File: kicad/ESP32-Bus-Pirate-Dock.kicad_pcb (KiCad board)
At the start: 4 copper layers, 80 x 73.8 mm, 39 parts, among them CN1 HX25418-10WA, J1 Conn_01x22, J2 Conn_01x22, J3 Conn_01x10V, J4 Conn_01x22, J5 Conn_01x22, J6 Conn_01x22, J7 Conn_02x03, Q1 2N7002, SW1 TA-3532S-A2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

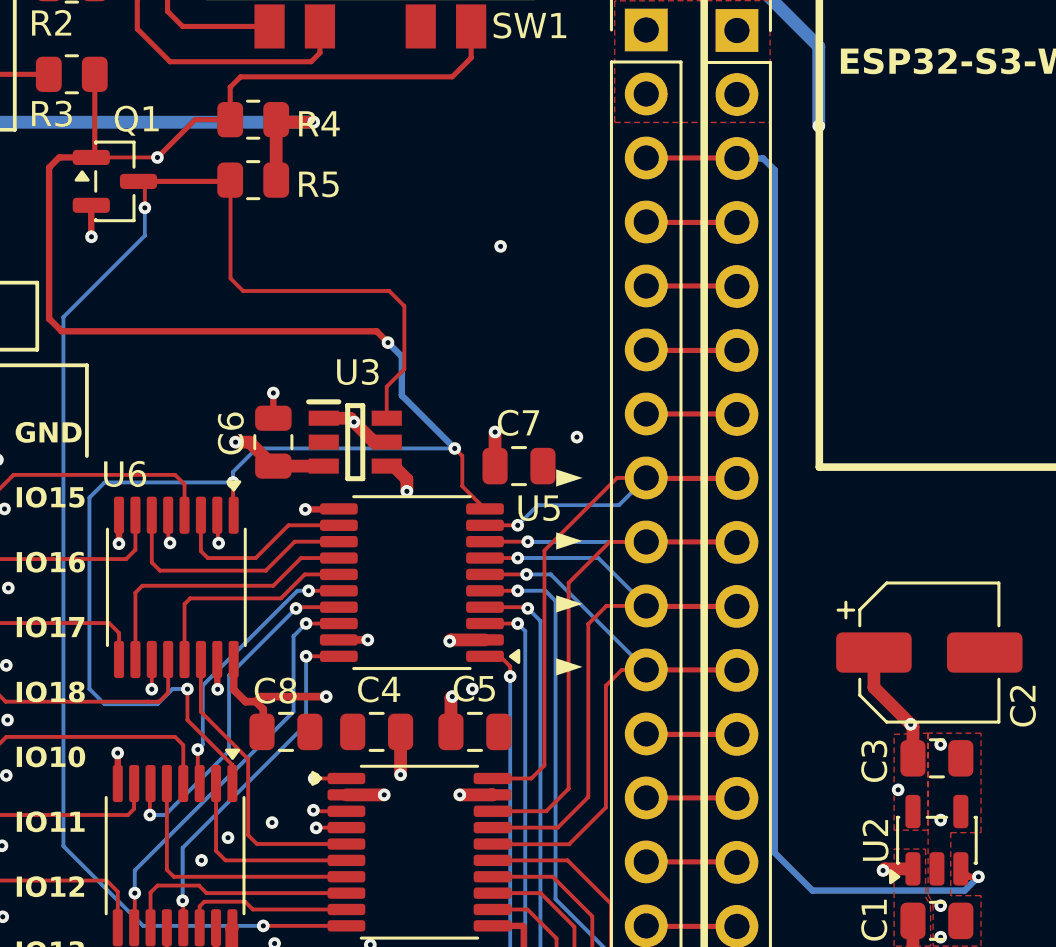
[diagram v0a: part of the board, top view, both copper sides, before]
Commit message: Deleted vias & added thermal relief spoke
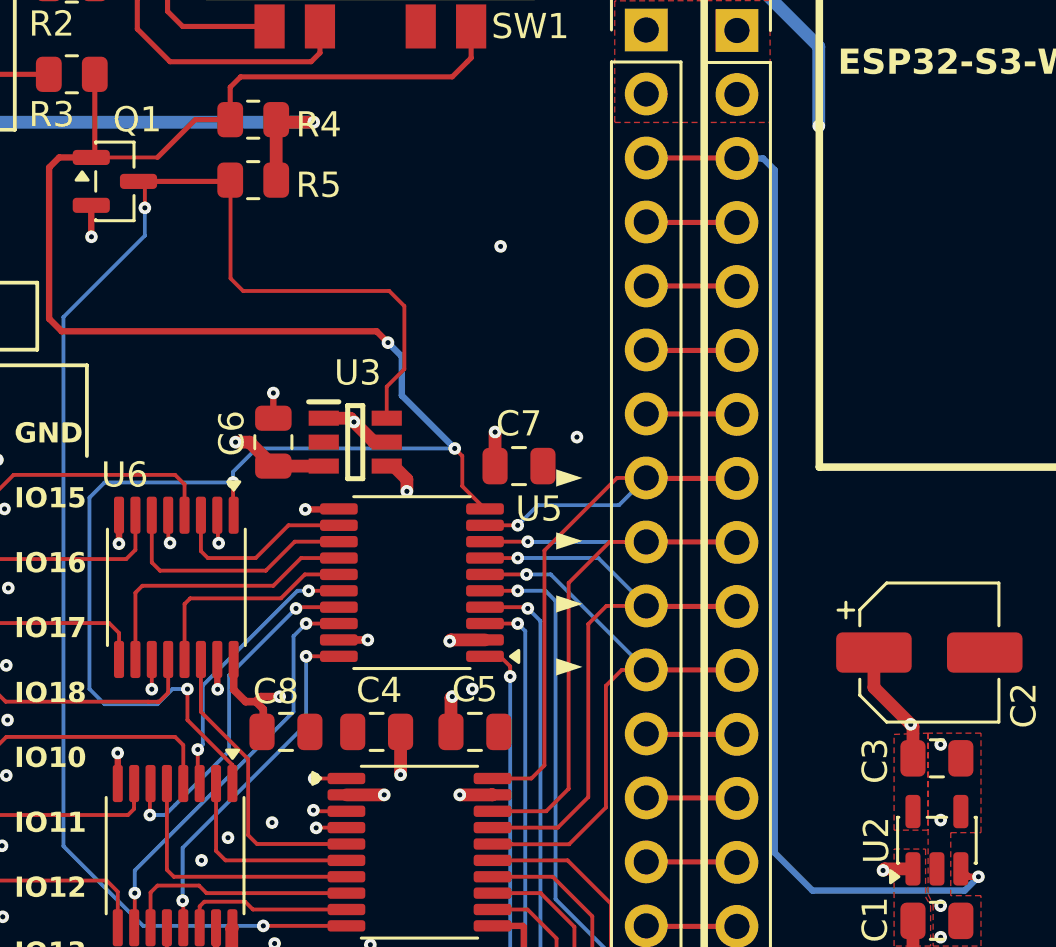
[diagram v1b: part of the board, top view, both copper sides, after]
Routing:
- net /Voltage Level Translator/SEL: vias 5 -> 4
- net +1V8: vias 7 -> 6
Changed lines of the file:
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@@
+	)
+	(segment
+		(start 152.45 96.9)
+		(end 151.7 96.9)
+		(width 0.3048)
+		(layer "F.Cu")
+		(net 11)
 	)
 	(segment
@@
 		(end 155.25 85.85)
 		(width 0.508)
-		(layer "F.Cu")
-		(net 11)
-	)
-	(segment
-		(start 151.7 96.9)
-		(end 154.3 96.9)
-		(width 0.3048)
 		(layer "F.Cu")
 		(net 11)
@@
 	)
 	(segment
+		(start 151.7 96.9)
+		(end 151.5 97.1)
+		(width 0.3048)
+		(layer "F.Cu")
+		(net 11)
+	)
+	(segment
 		(start 159.25 94.65)
 		(end 159.2 94.7)
@@
 		(net 11)
 	)
-	(segment
-		(start 151.5 97.1)
-		(end 151.7 96.9)
-		(width 0.3048)
-		(layer "F.Cu")
-		(net 11)
-	)
 	(via
 		(at 155.4 86)
@@
 	)
 	(via
-		(at 154.3 96.9)
+		(at 152.45 96.9)
 		(size 0.5)
 		(drill 0.2)
@@
 	)
 	(segment
+		(start 158.3 96.9)
+		(end 158.3 94.2)
+		(width 0.508)
+		(layer "In2.Cu")
+		(net 11)
+	)
+	(segment
+		(start 158.3 100)
+		(end 158.3 99.5)
+		(width 0.508)
+		(layer "In2.Cu")
+		(net 11)
+	)
+	(segment
+		(start 156.2 86.8)
+		(end 155.4 86)
+		(width 0.508)
+		(layer "In2.Cu")
+		(net 11)
+	)
+	(segment
+		(start 159.1 100.8)
+		(end 158.3 100)
+		(width 0.508)
+		(layer "In2.Cu")
+		(net 11)
+	)
+	(segment
+		(start 166.2 63)
+		(end 167 63.8)
+		(width 0.508)
+		(layer "In2.Cu")
+		(net 11)
+	)
+	(segment
+		(start 161 86.4)
+		(end 159.1 88.3)
+		(width 0.508)
+		(layer "In2.Cu")
+		(net 11)
+	)
+	(segment
+		(start 158 74.1)
+		(end 159.12 72.98)
+		(width 0.508)
+		(layer "In2.Cu")
+		(net 11)
+	)
+	(segment
+		(start 167 63.8)
+		(end 167 70.44)
+		(width 0.508)
+		(layer "In2.Cu")
+		(net 11)
+	)
+	(segment
+		(start 158.8 94.7)
+		(end 158.3 94.2)
+		(width 0.508)
+		(layer "In2.Cu")
+		(net 11)
+	)
+	(segment
+		(start 159.6 100.8)
+		(end 159.1 100.8)
+		(width 0.508)
+		(layer "In2.Cu")
+		(net 11)
+	)
+	(segment
+		(start 158.3 122.43)
+		(end 158.3 107.5)
+		(width 0.508)
+		(layer "In2.Cu")
+		(net 11)
+	)
+	(segment
+		(start 158.3 99.5)
+		(end 158.3 107.5)
+		(width 0.508)
+		(layer "In2.Cu")
+		(net 11)
+	)
+	(segment
+		(start 158.7 96.9)
+		(end 159.3 96.9)
+		(width 0.508)
+		(layer "In2.Cu")
+		(net 11)
+	)
+	(segment
+		(start 158.2 74.1)
+		(end 158 74.1)
+		(width 0.508)
+		(layer "In2.Cu")
+		(net 11)
+	)
+	(segment
+		(start 158.3 94.2)
+		(end 158.3 88.3)
+		(width 0.508)
+		(layer "In2.Cu")
+		(net 11)
+	)
+	(segment
+		(start 158.2 87.4)
+		(end 158.2 74.1)
+		(width 0.508)
+		(layer "In2.Cu")
+		(net 11)
+	)
+	(segment
+		(start 158.3 107.5)
+		(end 157.6 108.2)
+		(width 0.508)
+		(layer "In2.Cu")
+		(net 11)
+	)
+	(segment
+		(start 154.1 63)
+		(end 166.2 63)
+		(width 0.508)
+		(layer "In2.Cu")
+		(net 11)
+	)
+	(segment
 		(start 158.3 96.5)
 		(end 158.7 96.9)
@@
 	)
 	(segment
-		(start 158.3 96.9)
-		(end 158.3 94.2)
-		(width 0.508)
-		(layer "In2.Cu")
-		(net 11)
-	)
-	(segment
-		(start 158.3 100)
-		(end 158.3 99.5)
-		(width 0.508)
-		(layer "In2.Cu")
-		(net 11)
-	)
-	(segment
-		(start 156.2 86.8)
-		(end 155.4 86)
-		(width 0.508)
-		(layer "In2.Cu")
-		(net 11)
-	)
-	(segment
-		(start 159.1 100.8)
-		(end 158.3 100)
-		(width 0.508)
-		(layer "In2.Cu")
-		(net 11)
-	)
-	(segment
-		(start 166.2 63)
-		(end 167 63.8)
-		(width 0.508)
-		(layer "In2.Cu")
-		(net 11)
-	)
-	(segment
-		(start 161 86.4)
-		(end 159.1 88.3)
-		(width 0.508)
-		(layer "In2.Cu")
-		(net 11)
-	)
-	(segment
-		(start 154.3 96.9)
-		(end 157.9 96.9)
-		(width 0.508)
-		(layer "In2.Cu")
-		(net 11)
-	)
-	(segment
-		(start 158 74.1)
-		(end 159.12 72.98)
-		(width 0.508)
-		(layer "In2.Cu")
-		(net 11)
-	)
-	(segment
-		(start 167 63.8)
-		(end 167 70.44)
-		(width 0.508)
-		(layer "In2.Cu")
-		(net 11)
-	)
-	(segment
-		(start 158.8 94.7)
-		(end 158.3 94.2)
-		(width 0.508)
-		(layer "In2.Cu")
-		(net 11)
-	)
-	(segment
-		(start 159.6 100.8)
-		(end 159.1 100.8)
-		(width 0.508)
-		(layer "In2.Cu")
-		(net 11)
-	)
-	(segment
-		(start 158.3 122.43)
-		(end 158.3 107.5)
-		(width 0.508)
-		(layer "In2.Cu")
-		(net 11)
-	)
-	(segment
-		(start 158.3 99.5)
-		(end 158.3 107.5)
-		(width 0.508)
-		(layer "In2.Cu")
-		(net 11)
-	)
-	(segment
-		(start 158.2 74.1)
-		(end 158 74.1)
-		(width 0.508)
-		(layer "In2.Cu")
-		(net 11)
-	)
-	(segment
-		(start 158.3 94.2)
-		(end 158.3 88.3)
-		(width 0.508)
-		(layer "In2.Cu")
-		(net 11)
-	)
-	(segment
-		(start 158.2 87.4)
-		(end 158.2 74.1)
-		(width 0.508)
-		(layer "In2.Cu")
-		(net 11)
-	)
-	(segment
-		(start 158.3 107.5)
-		(end 157.6 108.2)
-		(width 0.508)
-		(layer "In2.Cu")
-		(net 11)
-	)
-	(segment
-		(start 154.1 63)
-		(end 166.2 63)
-		(width 0.508)
-		(layer "In2.Cu")
-		(net 11)
-	)
-	(segment
 		(start 158.3 88.3)
 		(end 158.3 87.5)
@@
 	)
 	(segment
-		(start 158.7 96.9)
-		(end 159.3 96.9)
+		(start 152.45 96.9)
+		(end 157.9 96.9)
 		(width 0.508)
 		(layer "In2.Cu")
@@
 	)
 	(segment
+		(start 158.2 87.4)
+		(end 157.6 86.8)
+		(width 0.508)
+		(layer "In2.Cu")
+		(net 11)
+	)
+	(segment
+		(start 158.3 99.5)
+		(end 158.3 96.9)
+		(width 0.508)
+		(layer "In2.Cu")
+		(net 11)
+	)
+	(segment
+		(start 159.12 72.98)
+		(end 167 72.98)
+		(width 0.508)
+		(layer "In2.Cu")
+		(net 11)
+	)
+	(segment
+		(start 159.2 94.7)
+		(end 158.8 94.7)
+		(width 0.508)
+		(layer "In2.Cu")
+		(net 11)
+	)
+	(segment
 		(start 157.9 96.9)
 		(end 158.3 96.5)
-		(width 0.508)
-		(layer "In2.Cu")
-		(net 11)
-	)
-	(segment
-		(start 158.2 87.4)
-		(end 157.6 86.8)
-		(width 0.508)
-		(layer "In2.Cu")
-		(net 11)
-	)
-	(segment
-		(start 158.3 99.5)
-		(end 158.3 96.9)
-		(width 0.508)
-		(layer "In2.Cu")
-		(net 11)
-	)
-	(segment
-		(start 159.12 72.98)
-		(end 167 72.98)
-		(width 0.508)
-		(layer "In2.Cu")
-		(net 11)
-	)
-	(segment
-		(start 159.2 94.7)
-		(end 158.8 94.7)
 		(width 0.508)
 		(layer "In2.Cu")
@@
 	)
 	(via
-		(at 177 100.6)
-		(size 0.5)
-		(drill 0.2)
-		(layers "F.Cu" "B.Cu")
-		(net 41)
-	)
-	(via
 		(at 160.05 65.95)
 		(size 0.5)
@@
 		(size 0.5)
 		(drill 0.2)
-		(layers "F.Cu" "B.Cu")
-		(net 56)
-	)
-	(via
-		(at 147.6 75.5)
-		(size 0.5)
-		(drill 0.2)
